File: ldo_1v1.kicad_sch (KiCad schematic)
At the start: 6 parts, among them U3 TPS7A20

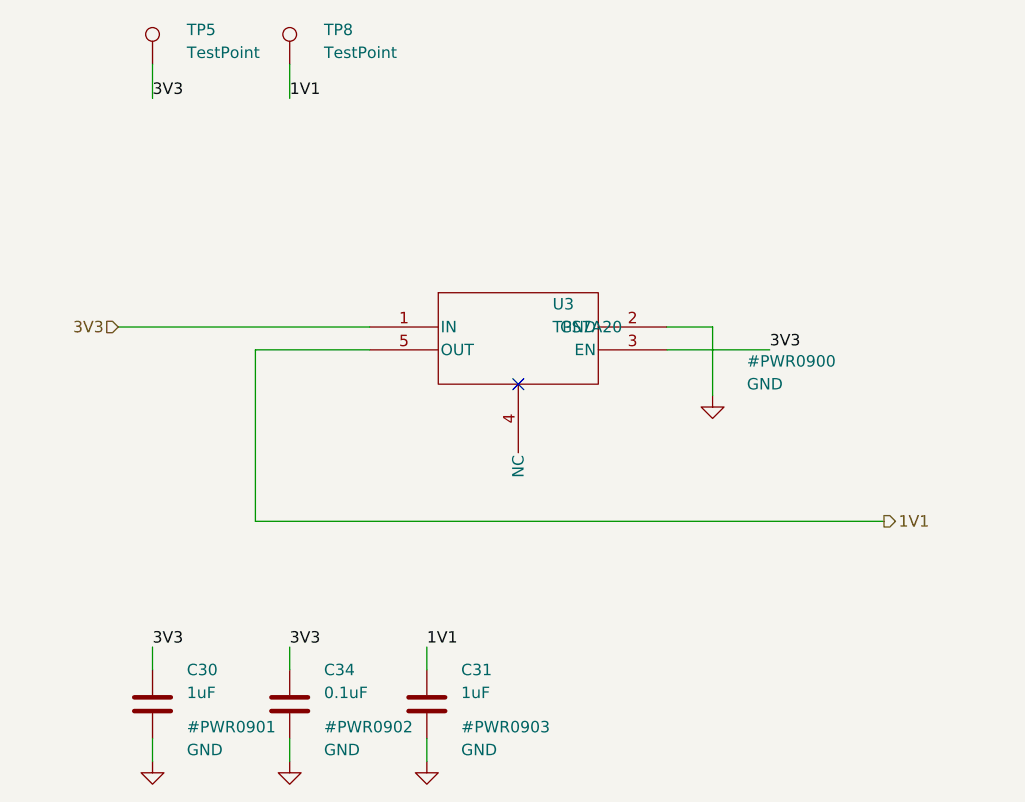
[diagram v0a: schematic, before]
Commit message: Migrate LDO sheets to KL library symbols
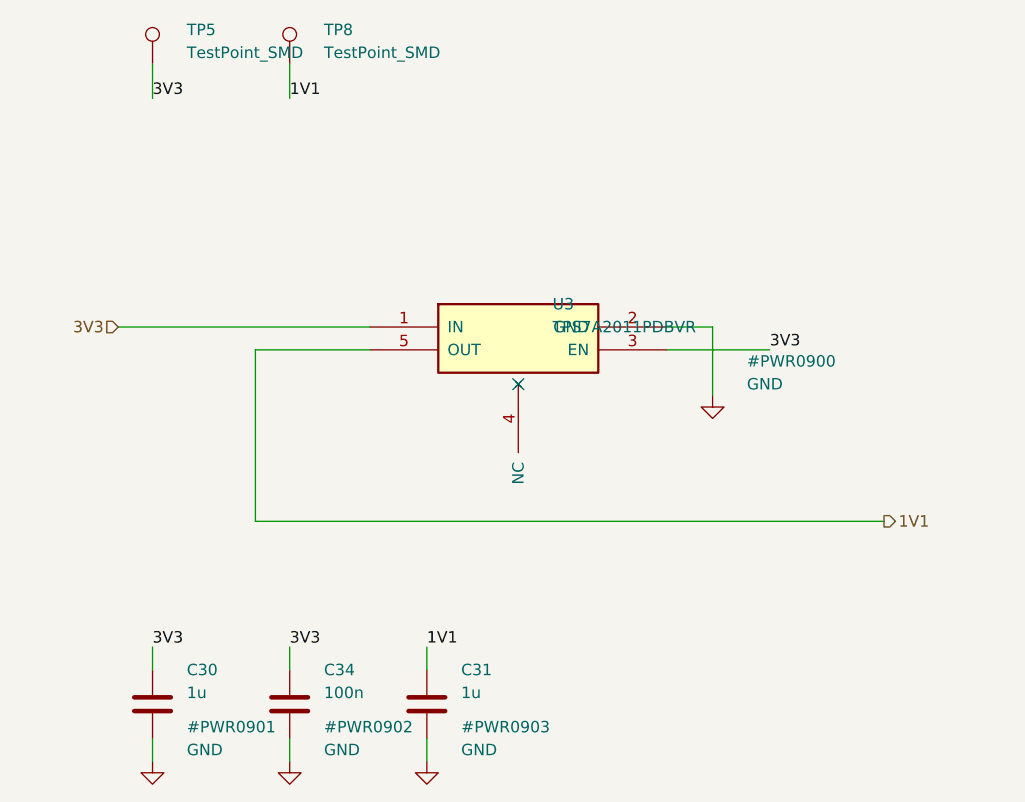
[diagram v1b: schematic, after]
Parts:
- C30, C31: value 1uF -> 1u; footprint Capacitor_SMD:C_0402_1005Metric_Pad0.74x0.62mm_HandSolder -> KL_Footprints:C_0402; symbol Device:C -> KL_C:C_1u_16V_10pct_X5R_0402; Dielectric (none) -> X5R; Digikey (none) -> TBD; LCSC (none) -> TBD; MPN (none) -> GRM155R61C105KA12D; Mouser (none) -> 81-GRM155R61C105KA12D; Package_in_inch (none) -> 0402; Tolerance_in_pct (none) -> 10; Voltage_in_V (none) -> 16
- C34: value 0.1uF -> 100n; footprint Capacitor_SMD:C_0402_1005Metric_Pad0.74x0.62mm_HandSolder -> KL_Footprints:C_0402; symbol Device:C -> KL_C:C_100n_35V_10pct_X7R_0402; Dielectric (none) -> X7R; Digikey (none) -> 445-6901-1-ND; LCSC (none) -> C2181802; MPN (none) -> CGA2B3X7R1V104K050BB; Mouser (none) -> 810-CGA2B3X7R1V104K; Package_in_inch (none) -> 0402; Tolerance_in_pct (none) -> 10; Voltage_in_V (none) -> 35
- TP5, TP8: value TestPoint -> TestPoint_SMD; footprint TestPoint:TestPoint_Pad_1.0x1.0mm -> KL_Footprints:TestPoint_SMD_1.0x1.0mm; symbol Connector:TestPoint -> KL_TestPoint:TestPoint_SMD
- U3: value TPS7A20 -> TPS7A2011PDBVR; footprint Package_TO_SOT_SMD:SOT-23-5 -> KL_Footprints:SOT-23-5; symbol TPS7A20C:TPS7A20C285PYCKR -> KL_Voltage_Regulators:TPS7A2011PDBVR; Digikey (none) -> TBD; I_OUT_A (none) -> 0.3; I_VIN_A (none) -> TBD; LCSC (none) -> TBD; MPN (none) -> TPS7A2011PDBVR; Mouser (none) -> 595-TPS7A2011PDBVR; VIN_MAX_V (none) -> 6.5; VIN_MIN_V (none) -> 1.6; V_OUT_V (none) -> 1.1

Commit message: Apply signal naming convention to all nets
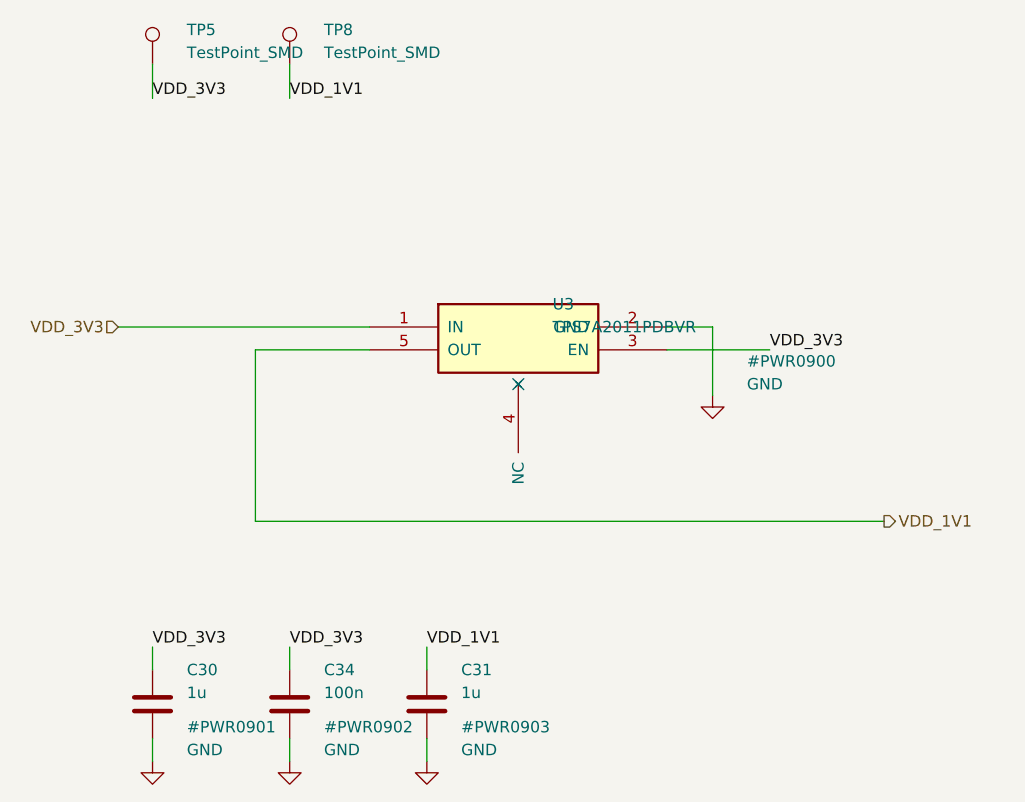
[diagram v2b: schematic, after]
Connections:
- net 1V1 renamed VDD_1V1
- net 3V3 renamed VDD_3V3
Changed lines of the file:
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@@
 		)
 	)
-	(hierarchical_label "3V3"
+	(hierarchical_label "VDD_3V3"
 		(shape input)
 		(at 96.52 88.9 180)
@@
 		)
 	)
-	(hierarchical_label "1V1"
+	(hierarchical_label "VDD_1V1"
 		(shape output)
 		(at 181.61 110.49 0)
@@
 		)
 	)
-	(label "3V3"
+	(label "VDD_3V3"
 		(at 168.91 91.44 0)
 		(effects
@@
 		)
 	)
-	(label "3V3"
+	(label "VDD_3V3"
 		(at 100.33 124.46 0)
 		(effects
@@
 		)
 	)
-	(label "3V3"
+	(label "VDD_3V3"
 		(at 115.57 124.46 0)
 		(effects
@@
 		)
 	)
-	(label "1V1"
+	(label "VDD_1V1"
 		(at 130.81 124.46 0)
 		(effects
@@
 		)
 	)
-	(label "3V3"
+	(label "VDD_3V3"
 		(at 100.33 63.5 0)
 		(effects
@@
 		)
 	)
-	(label "1V1"
+	(label "VDD_1V1"
 		(at 115.57 63.5 0)
 		(effects

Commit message: Improve schematic readability across all sheets
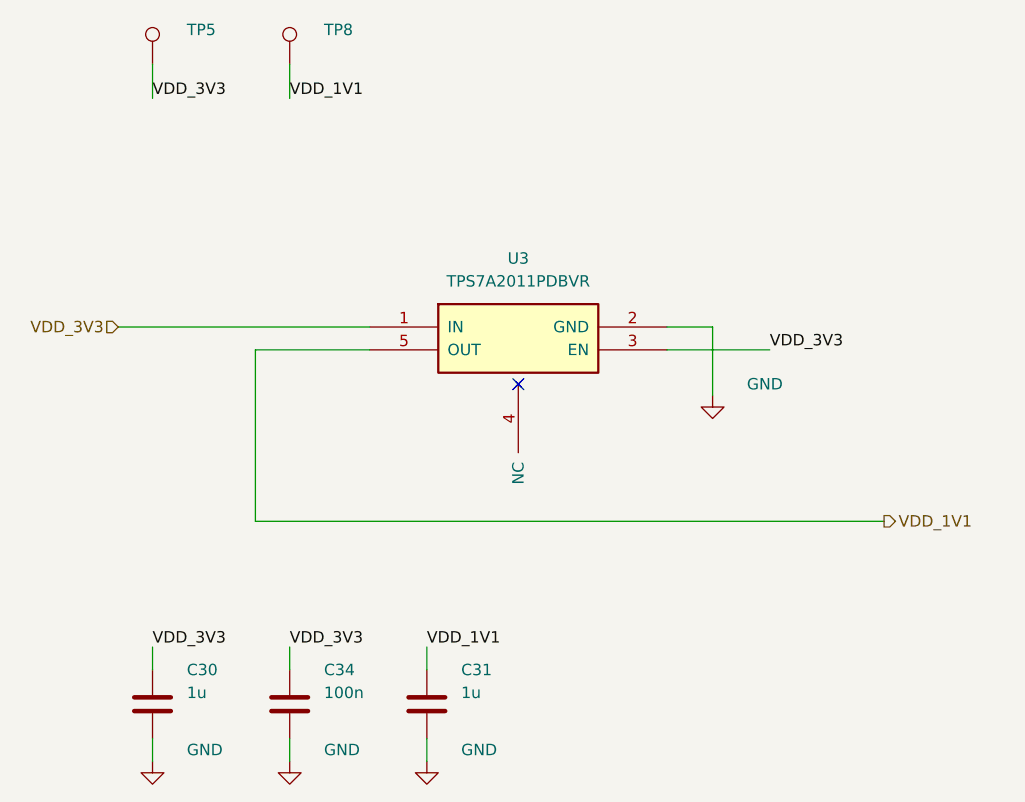
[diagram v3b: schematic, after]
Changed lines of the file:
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@@
 		(dnp no)
 		(property "Reference" "U3"
-			(at 144.78 86.36 0)
-			(effects
-				(font
-					(size 1.27 1.27)
-				)
-				(justify left)
+			(at 140.97 81.28 0)
+			(effects
+				(font
+					(size 1.27 1.27)
+				)
 			)
 		)
 		(property "Value" "TPS7A2011PDBVR"
-			(at 144.78 88.9 0)
-			(effects
-				(font
-					(size 1.27 1.27)
-				)
-				(justify left)
+			(at 140.97 83.82 0)
+			(effects
+				(font
+					(size 1.27 1.27)
+				)
 			)
 		)
@@
 		(property "Reference" "#PWR0900"
 			(at 166.37 92.71 0)
+			(hide yes)
 			(effects
 				(font
@@
 		(property "Reference" "#PWR0901"
 			(at 104.14 133.35 0)
+			(hide yes)
 			(effects
 				(font
@@
 		(property "Reference" "#PWR0902"
 			(at 119.38 133.35 0)
+			(hide yes)
 			(effects
 				(font
@@
 		(property "Reference" "#PWR0903"
 			(at 134.62 133.35 0)
+			(hide yes)
 			(effects
 				(font
@@
 		(property "Value" "TestPoint_SMD"
 			(at 104.14 58.419999999999995 0)
+			(hide yes)
 			(effects
 				(font
@@
 		(property "Value" "TestPoint_SMD"
 			(at 119.38 58.419999999999995 0)
-			(effects
-				(font
+			(hide yes)
+			(effects
+				(font

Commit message: Move 1V1 LDO ground symbol; KiCad 10 format
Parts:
- C30, C31: Digikey TBD -> 490-10694-1-ND; LCSC TBD -> C77006
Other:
- company: (none) -> Kebag Logic: kebag-logic.com
- title: (none) -> LDO 1V1

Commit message: Switch BOM to in-stock LCSC parts, U3 to TLV73311
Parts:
- C34: Digikey 445-6901-1-ND -> (none); LCSC C2181802 -> C307331; MPN CGA2B3X7R1V104K050BB -> CL05B104KB54PNC; Mouser 810-CGA2B3X7R1V104K -> (none); Voltage_in_V 35 -> 50
- U3: value TPS7A2011PDBVR -> TLV73311PDBVR; Digikey TBD -> (none); LCSC TBD -> C2865431; MPN TPS7A2011PDBVR -> TLV73311PDBVR; Mouser 595-TPS7A2011PDBVR -> (none)
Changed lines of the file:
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@@
 			)
 		)
-		(property "Datasheet" "https://product.tdk.com/system/files/dam/doc/product/capacitor/ceramic/mlcc/catalog/mlcc_automotive_general_en.pdf"
+		(property "Datasheet" "https://www.lcsc.com/datasheet/lcsc_datasheet_2304140030_Samsung-Electro-Mechanics-CL05B104KB54PNC_C307331.pdf"
 			(at 119.38 134.62 0)
 			(hide yes)
@@
 			)
 		)
-		(property "Voltage_in_V" "35"
+		(property "Voltage_in_V" "50"
 			(at 0 0 0)
 			(hide yes)
@@
 			)
 		)
-		(property "MPN" "CGA2B3X7R1V104K050BB"
-			(at 0 0 0)
-			(hide yes)
-			(show_name no)
-			(do_not_autoplace no)
-			(effects
-				(font
-					(size 1.27 1.27)
-				)
-			)
-		)
-		(property "Mouser" "810-CGA2B3X7R1V104K"
-			(at 0 0 0)
-			(hide yes)
-			(show_name no)
-			(do_not_autoplace no)
-			(effects
-				(font
-					(size 1.27 1.27)
-				)
-			)
-		)
-		(property "Digikey" "445-6901-1-ND"
-			(at 0 0 0)
-			(hide yes)
-			(show_name no)
-			(do_not_autoplace no)
-			(effects
-				(font
-					(size 1.27 1.27)
-				)
-			)
-		)
-		(property "LCSC" "C2181802"
+		(property "MPN" "CL05B104KB54PNC"
+			(at 0 0 0)
+			(hide yes)
+			(show_name no)
+			(do_not_autoplace no)
+			(effects
+				(font
+					(size 1.27 1.27)
+				)
+			)
+		)
+		(property "Mouser" ""
+			(at 0 0 0)
+			(hide yes)
+			(show_name no)
+			(do_not_autoplace no)
+			(effects
+				(font
+					(size 1.27 1.27)
+				)
+			)
+		)
+		(property "Digikey" ""
+			(at 0 0 0)
+			(hide yes)
+			(show_name no)
+			(do_not_autoplace no)
+			(effects
+				(font
+					(size 1.27 1.27)
+				)
+			)
+		)
+		(property "LCSC" "C307331"
 			(at 0 0 0)
 			(hide yes)
@@
 			)
 		)
-		(property "Value" "TPS7A2011PDBVR"
+		(property "Value" "TLV73311PDBVR"
 			(at 140.97 83.82 0)
 			(show_name no)
@@
 			)
 		)
-		(property "Datasheet" "https://www.ti.com/lit/gpn/tps7a20"
+		(property "Datasheet" "https://www.ti.com/lit/ds/symlink/tlv733p.pdf"
 			(at 144.78 93.98 0)
 			(hide yes)
@@
 			)
 		)
-		(property "MPN" "TPS7A2011PDBVR"
-			(at 0 0 0)
-			(hide yes)
-			(show_name no)
-			(do_not_autoplace no)
-			(effects
-				(font
-					(size 1.27 1.27)
-				)
-			)
-		)
-		(property "Mouser" "595-TPS7A2011PDBVR"
-			(at 0 0 0)
-			(hide yes)
-			(show_name no)
-			(do_not_autoplace no)
-			(effects
-				(font
-					(size 1.27 1.27)
-				)
-			)
-		)
-		(property "Digikey" "TBD"
-			(at 0 0 0)
-			(hide yes)
-			(show_name no)
-			(do_not_autoplace no)
-			(effects
-				(font
-					(size 1.27 1.27)
-				)
-			)
-		)
-		(property "LCSC" "TBD"
-			(at 0 0 0)
-			(hide yes)
+		(property "MPN" "TLV73311PDBVR"
+			(at 0 0 0)
+			(hide yes)
+			(show_name no)
+			(do_not_autoplace no)
+			(effects
+				(font
+					(size 1.27 1.27)
+				)
+			)
+		)
+		(property "Mouser" ""
+			(at 0 0 0)
+			(hide yes)
+			(show_name no)
+			(do_not_autoplace no)
+			(effects
+				(font
+					(size 1.27 1.27)
+				)
+			)
+		)
+		(property "Digikey" ""
+			(at 0 0 0)
+			(hide yes)
+			(show_name no)
+			(do_not_autoplace no)
+			(effects
+				(font
+					(size 1.27 1.27)
+				)
+			)
+		)
+		(property "LCSC" "C2865431"
+			(at 0 0 0)
+			(hide yes)
